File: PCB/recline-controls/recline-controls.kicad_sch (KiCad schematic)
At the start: 0 parts

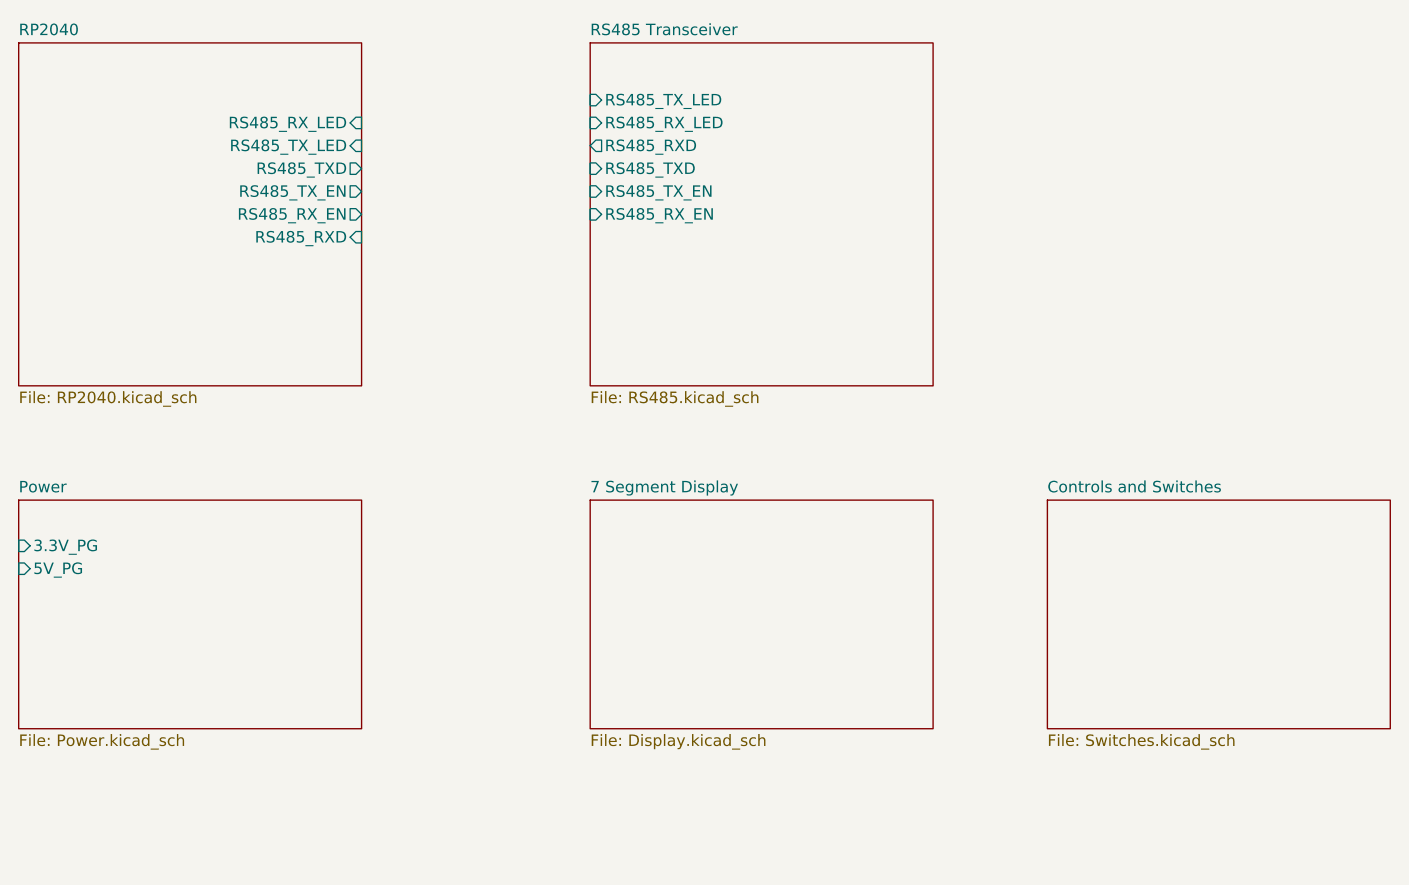
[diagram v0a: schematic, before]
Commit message: Recline Controls
Recline Control board and human machine interface board schematic complete !
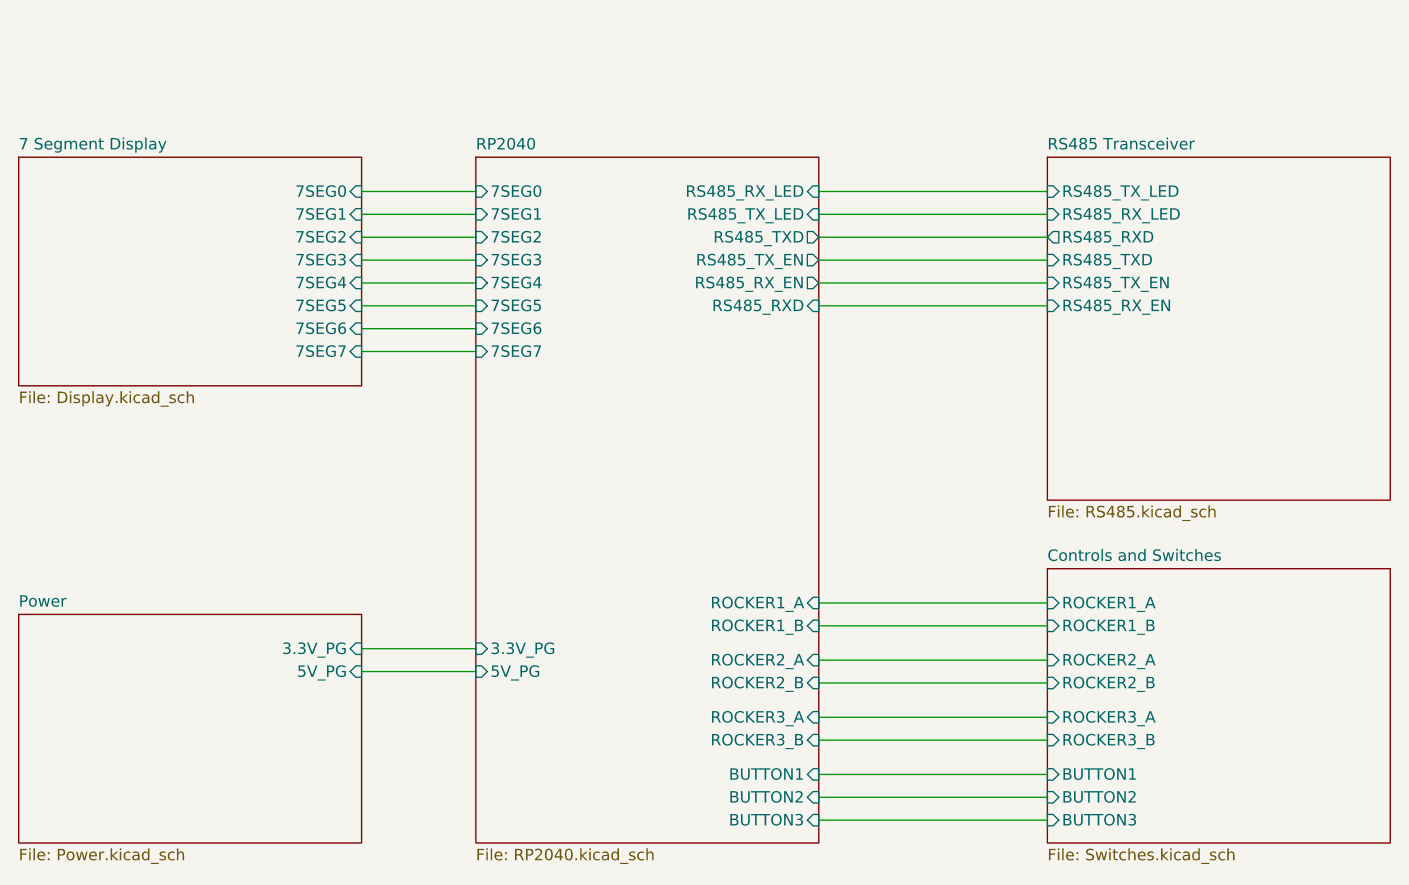
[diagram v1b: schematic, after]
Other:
- sheet 7 Segment Display ports: added 7SEG0, 7SEG1, 7SEG2, 7SEG3, 7SEG4, 7SEG5, 7SEG6, 7SEG7; removed none
- sheet Controls and Switches ports: added BUTTON1, BUTTON2, BUTTON3, ROCKER1_A, ROCKER1_B, ROCKER2_A, ROCKER2_B, ROCKER3_A, ROCKER3_B; removed none
- sheet RP2040 ports: added 3.3V_PG, 5V_PG, 7SEG0, 7SEG1, 7SEG2, 7SEG3, 7SEG4, 7SEG5, 7SEG6, 7SEG7, BUTTON1, BUTTON2, BUTTON3, ROCKER1_A, ROCKER1_B, ROCKER2_A, ROCKER2_B, ROCKER3_A, ROCKER3_B; removed none

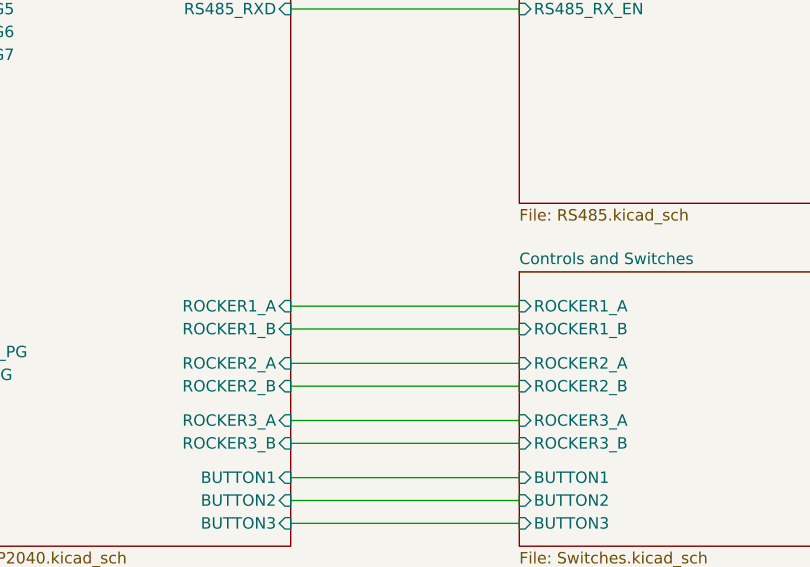
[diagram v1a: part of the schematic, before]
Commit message: All Hardware Tweaked / 3D Renders
PCBs for Actuator Control, Recline Control HID, and 7 Segment carrier are all complete with full 3D models rendering. 3D Renders of all board added to repository img directory.
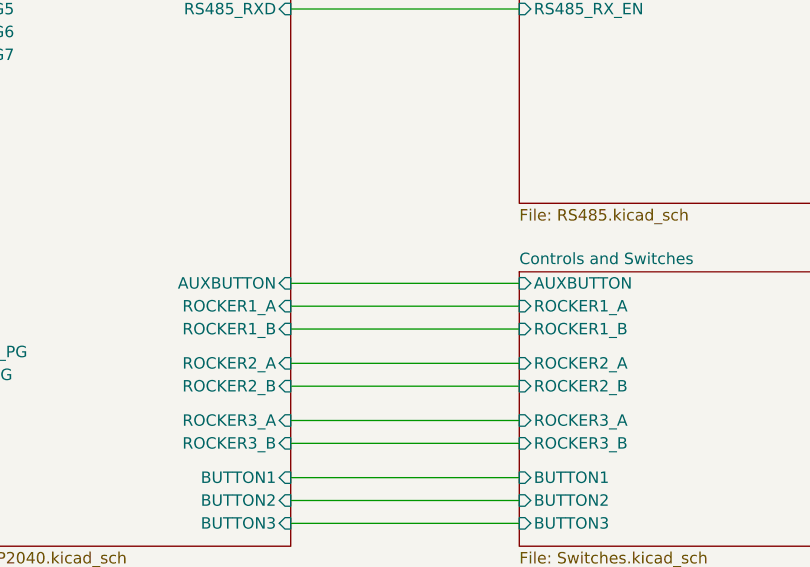
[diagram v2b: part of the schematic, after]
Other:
- sheet Controls and Switches ports: added AUXBUTTON; removed none
- sheet RP2040 ports: added AUXBUTTON; removed none
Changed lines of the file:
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@@
+	(wire
+		(pts
+			(xy 165.1 97.79) (xy 190.5 97.79)
+		)
+		(stroke
+			(width 0)
+			(type default)
+		)
+	)
 	(wire
 		(pts
@@
 			)
 		)
+		(pin "AUXBUTTON" input
+			(at 190.5 97.79 180)
+			(effects
+				(font
+					(size 1.27 1.27)
+				)
+				(justify left)
+			)
+		)
 		(instances
 			(project "recline-controls"
@@
 			)
 		)
+		(pin "AUXBUTTON" input
+			(at 165.1 97.79 0)
+			(effects
+				(font
+					(size 1.27 1.27)
+				)
+				(justify right)
+			)
+		)

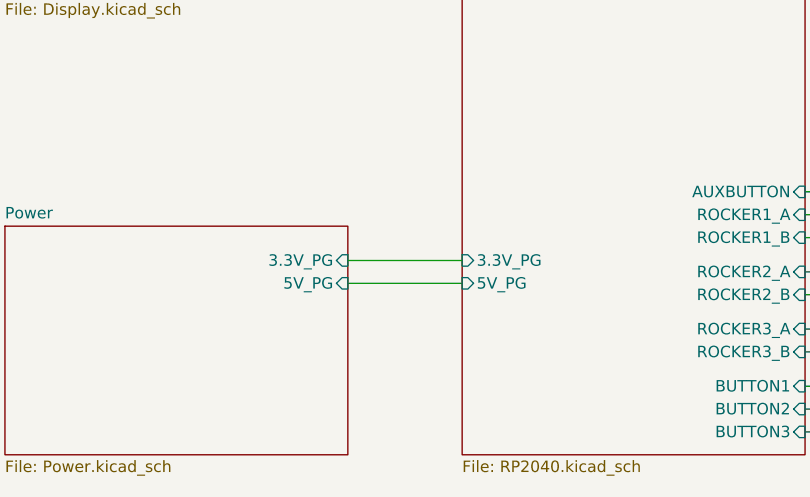
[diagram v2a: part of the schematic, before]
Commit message: HID
Changes made to recline control HID board. Power input section redesigned, 5V regulator removed, RS485 circuit updated with fixes that other boards received. Redesign or internal plane topology following changes to RS485 section. Via stitching all around.
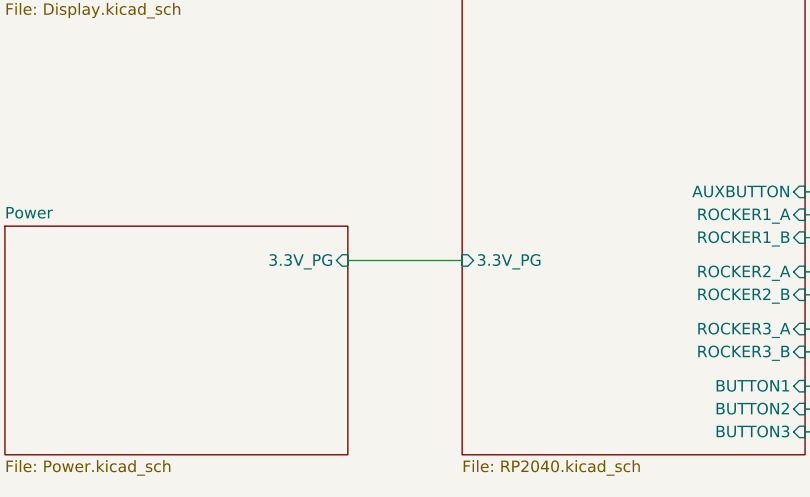
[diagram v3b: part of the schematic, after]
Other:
- sheet Power ports: added none; removed 5V_PG
- sheet RP2040 ports: added none; removed 5V_PG
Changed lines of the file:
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@@
-	(wire
-		(pts
-			(xy 114.3 107.95) (xy 127 107.95)
-		)
-		(stroke
-			(width 0)
-			(type default)
-		)
-	)
 	(wire
 		(pts
@@
 			)
 		)
-		(pin "5V_PG" input
-			(at 127 107.95 180)
-			(effects
-				(font
-					(size 1.27 1.27)
-				)
-				(justify left)
-			)
-		)
 		(pin "3.3V_PG" input
 			(at 127 105.41 180)
@@
 			(effects
 				(font
-					(size 1.27 1.27)
-				)
-				(justify right)
-			)
-		)
-		(pin "5V_PG" input
-			(at 114.3 107.95 0)
-			(effects
-				(font
